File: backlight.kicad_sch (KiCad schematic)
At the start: 56 parts

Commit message: all unit test pass
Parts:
- LED11, LED12, LED13, LED21, LED22, LED23, LED31, LED32, LED33, LED41, LED42, LED43, LED51, LED52, LED53, LED61, LED62, LED63, LED71, LED72, LED73, LED81, LED82, LED83: value Белый SMD 0805 -> Белый SMD 1206
- LED201, LED202, LED203, LED204, LED205, LED206, LED207, LED208, LED209, LED210, LED211, LED212: value Белый SMD 0603 -> Белый SMD 1206
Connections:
- net GND: now also LED103.1 (K), LED106.1 (K), LED13.1 (K), LED203.1 (K), LED206.1 (K), LED209.1 (K), LED212.1 (K), LED23.1 (K), LED33.1 (K), LED43.1 (K), LED53.1 (K), LED63.1 (K), LED73.1 (K), LED83.1 (K); no longer LED103.2 (A), LED106.2 (A), LED13.2 (A), LED203.2 (A), LED206.2 (A), LED209.2 (A), LED212.2 (A), LED23.2 (A), LED33.2 (A), LED43.2 (A), LED53.2 (A), LED63.2 (A), LED73.2 (A), LED83.2 (A)
- net NET_BTN_CH1_A: now also LED101.2 (A); no longer LED101.1 (K)
- net NET_BTN_CH1_B: now also LED101.1 (K), LED102.2 (A); no longer LED101.2 (A), LED102.1 (K)
- net NET_BTN_CH1_C: now also LED102.1 (K), LED103.2 (A); no longer LED102.2 (A), LED103.1 (K)
- net NET_BTN_CH2_A: now also LED104.2 (A); no longer LED104.1 (K)
- net NET_BTN_CH2_B: now also LED104.1 (K), LED105.2 (A); no longer LED104.2 (A), LED105.1 (K)
- net NET_BTN_CH2_C: now also LED105.1 (K), LED106.2 (A); no longer LED105.2 (A), LED106.1 (K)
- net NET_PTR_CH1_A: now also LED201.2 (A); no longer LED201.1 (K)
- net NET_PTR_CH1_B: now also LED201.1 (K), LED202.2 (A); no longer LED201.2 (A), LED202.1 (K)
- net NET_PTR_CH1_C: now also LED202.1 (K), LED203.2 (A); no longer LED202.2 (A), LED203.1 (K)
- net NET_PTR_CH2_A: now also LED204.2 (A); no longer LED204.1 (K)
- net NET_PTR_CH2_B: now also LED204.1 (K), LED205.2 (A); no longer LED204.2 (A), LED205.1 (K)
- net NET_PTR_CH2_C: now also LED205.1 (K), LED206.2 (A); no longer LED205.2 (A), LED206.1 (K)
- net NET_PTR_CH3_A: now also LED207.2 (A); no longer LED207.1 (K)
- net NET_PTR_CH3_B: now also LED207.1 (K), LED208.2 (A); no longer LED207.2 (A), LED208.1 (K)
- net NET_PTR_CH3_C: now also LED208.1 (K), LED209.2 (A); no longer LED208.2 (A), LED209.1 (K)
- net NET_PTR_CH4_A: now also LED210.2 (A); no longer LED210.1 (K)
- net NET_PTR_CH4_B: now also LED210.1 (K), LED211.2 (A); no longer LED210.2 (A), LED211.1 (K)
- net NET_PTR_CH4_C: now also LED211.1 (K), LED212.2 (A); no longer LED211.2 (A), LED212.1 (K)
- net NET_SCALE_CH1_A: now also LED11.2 (A); no longer LED11.1 (K)
- net NET_SCALE_CH1_B: now also LED11.1 (K), LED12.2 (A); no longer LED11.2 (A), LED12.1 (K)
- net NET_SCALE_CH1_C: now also LED12.1 (K), LED13.2 (A); no longer LED12.2 (A), LED13.1 (K)
- net NET_SCALE_CH2_A: now also LED21.2 (A); no longer LED21.1 (K)
- net NET_SCALE_CH2_B: now also LED21.1 (K), LED22.2 (A); no longer LED21.2 (A), LED22.1 (K)
- net NET_SCALE_CH2_C: now also LED22.1 (K), LED23.2 (A); no longer LED22.2 (A), LED23.1 (K)
- net NET_SCALE_CH3_A: now also LED31.2 (A); no longer LED31.1 (K)
- net NET_SCALE_CH3_B: now also LED31.1 (K), LED32.2 (A); no longer LED31.2 (A), LED32.1 (K)
- net NET_SCALE_CH3_C: now also LED32.1 (K), LED33.2 (A); no longer LED32.2 (A), LED33.1 (K)
- net NET_SCALE_CH4_A: now also LED41.2 (A); no longer LED41.1 (K)
- net NET_SCALE_CH4_B: now also LED41.1 (K), LED42.2 (A); no longer LED41.2 (A), LED42.1 (K)
- net NET_SCALE_CH4_C: now also LED42.1 (K), LED43.2 (A); no longer LED42.2 (A), LED43.1 (K)
- net NET_SCALE_CH5_A: now also LED51.2 (A); no longer LED51.1 (K)
- net NET_SCALE_CH5_B: now also LED51.1 (K), LED52.2 (A); no longer LED51.2 (A), LED52.1 (K)
- net NET_SCALE_CH5_C: now also LED52.1 (K), LED53.2 (A); no longer LED52.2 (A), LED53.1 (K)
- net NET_SCALE_CH6_A: now also LED61.2 (A); no longer LED61.1 (K)
- net NET_SCALE_CH6_B: now also LED61.1 (K), LED62.2 (A); no longer LED61.2 (A), LED62.1 (K)
- net NET_SCALE_CH6_C: now also LED62.1 (K), LED63.2 (A); no longer LED62.2 (A), LED63.1 (K)
- net NET_SCALE_CH7_A: now also LED71.2 (A); no longer LED71.1 (K)
- net NET_SCALE_CH7_B: now also LED71.1 (K), LED72.2 (A); no longer LED71.2 (A), LED72.1 (K)
- net NET_SCALE_CH7_C: now also LED72.1 (K), LED73.2 (A); no longer LED72.2 (A), LED73.1 (K)
- net NET_SCALE_CH8_A: now also LED81.2 (A); no longer LED81.1 (K)
- net NET_SCALE_CH8_B: now also LED81.1 (K), LED82.2 (A); no longer LED81.2 (A), LED82.1 (K)
- net NET_SCALE_CH8_C: now also LED82.1 (K), LED83.2 (A); no longer LED82.2 (A), LED83.1 (K)

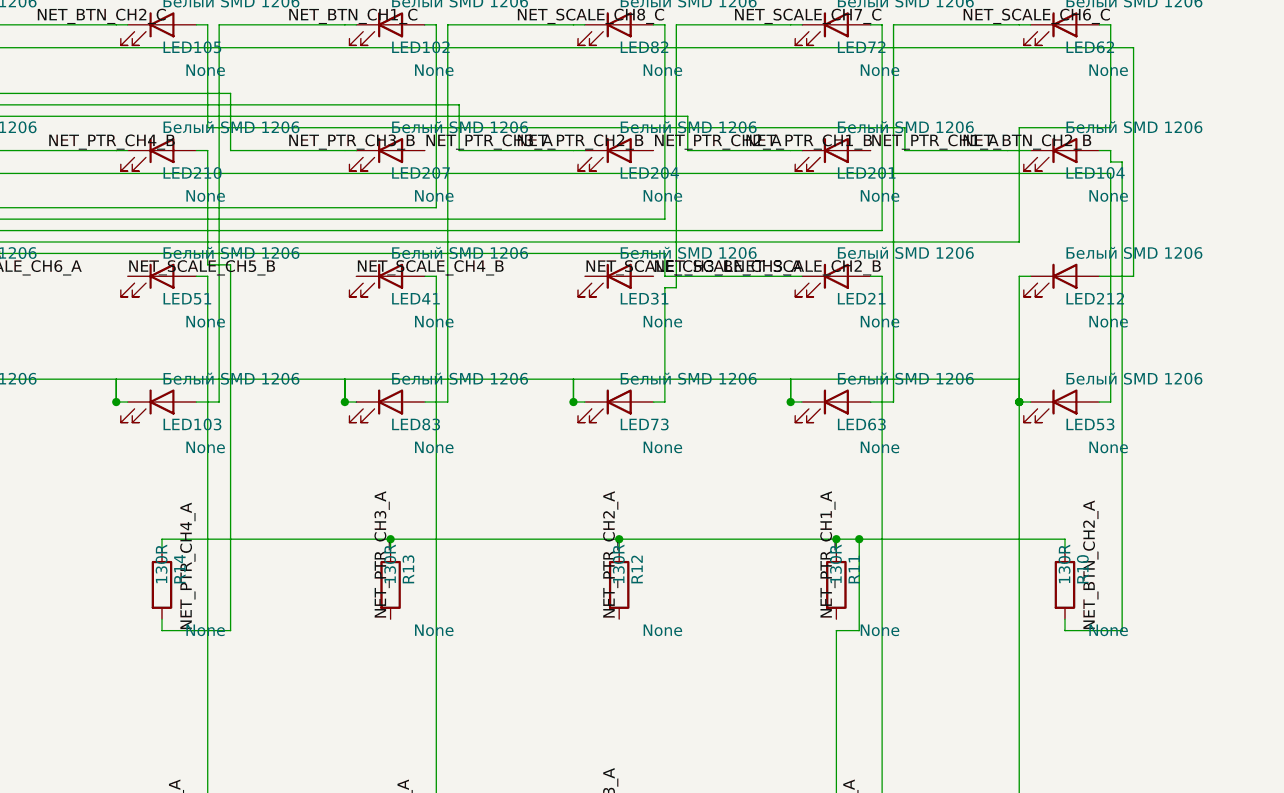
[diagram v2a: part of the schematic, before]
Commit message: optimazed load to kicad
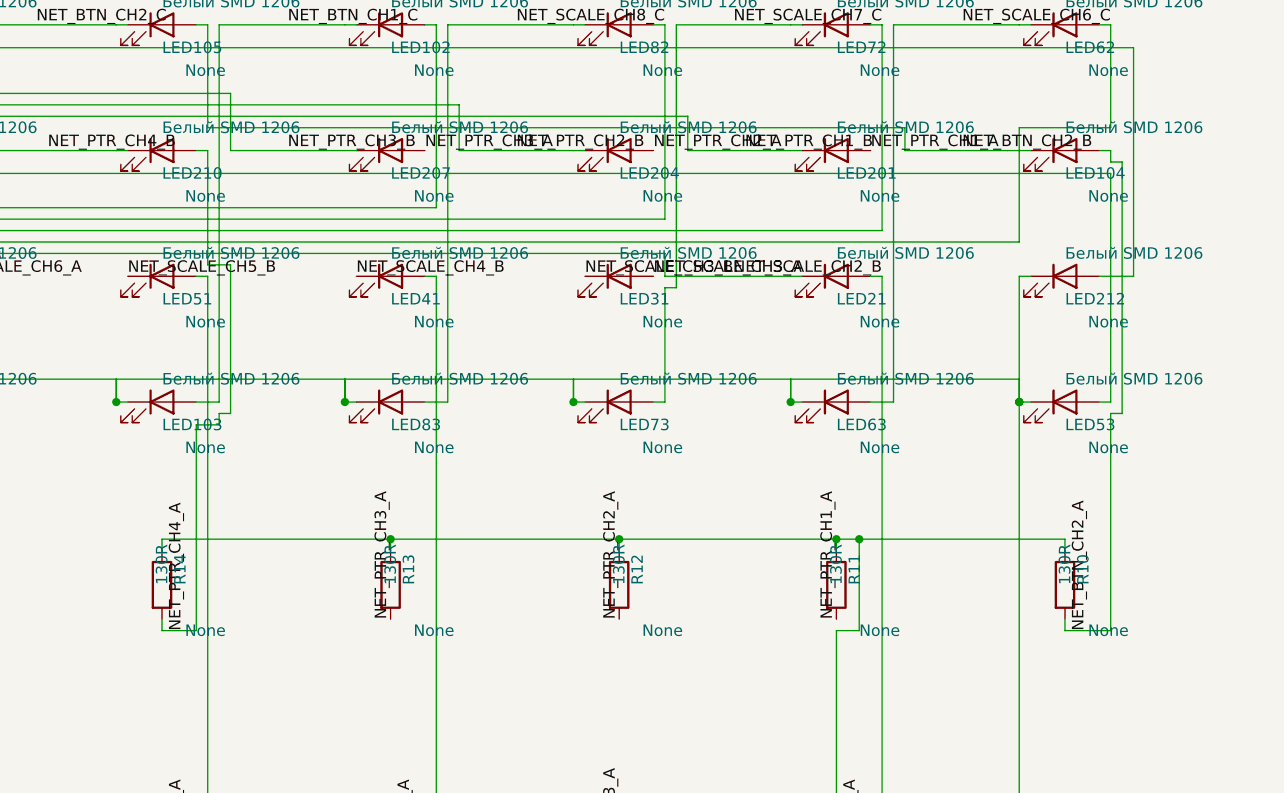
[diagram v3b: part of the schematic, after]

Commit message: tests_fix
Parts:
- LED101, LED102, LED103, LED104, LED105, LED106, LED11, LED12, LED13, LED201, LED202, LED203, LED204, LED205, LED206, LED207, LED208, LED209, LED21, LED210, LED211, LED212, LED22, LED23, LED31, LED32, LED33, LED41, LED42, LED43, LED51, LED52, LED53, LED61, LED62, LED63, LED71, LED72, LED73, LED81, LED82, LED83, R1, R10, R11, R12, R13, R14, R2, R3, R4, R5, R6, R7, R8, R9: hierarchy_path (none) -> /c5a034c1-1f54-4e7e-8711-0930d2b4314e/96464050-9378-46b5-82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
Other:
- title: (none) -> climate_control_niva_travel

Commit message: refactoring
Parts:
- LED101, LED102, LED103, LED104, LED105, LED106, LED11, LED12, LED13, LED201, LED202, LED203, LED204, LED205, LED206, LED207, LED208, LED209, LED21, LED210, LED211, LED212, LED22, LED23, LED31, LED32, LED33, LED41, LED42, LED43, LED51, LED52, LED53, LED61, LED62, LED63, LED71, LED72, LED73, LED81, LED82, LED83, R1, R10, R11, R12, R13, R14, R2, R3, R4, R5, R6, R7, R8, R9: hierarchy_path /c5a034c1-1f54-4e7e-8711-0930d2b4314e/96464050-9378-46b5-82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 -> (none)
